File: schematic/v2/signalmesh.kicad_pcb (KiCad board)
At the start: 4 copper layers, 387 x 151 mm, 188 parts, among them J1 FPGA I/O, J10 INA219_CONFIG, J11 INA219_CONFIG, J12 AAM_DBG, J13 UUM_DBG, J14 ACM_DBG, J15 INA219_CONFIG, J16 DSM_DBG, J17 LCD_display, J18 LCD_display, J19 AudioJack3, J2 FPGA I/O, J20 USB_A, J21 USB_A, J22 USB_A, J23 USB_A, J3 LCD_display, J4 TDM_DBG, J5 INA219_CONFIG, J6 INA219_CONFIG, J7 INA219_CONFIG, J8 FPGA I/O, J9 FPGA I/O, U1 NUCLEO-H753ZI, U10 INA219AxD, U11 INA219AxD, U12 INA219AxD, U13 INA219AxD, U14 W25Q128JVS, U15 AP2112K-3.3, U16 74HC4050D, U17 NUCLEO-H753ZI, U18 HDSP-7503, U19 HDSP-7503, U2 HDSP-7503, U20 INA219AxD, U21 74HC4050D, U22 AP2112K-3.3, U23 W25Q128JVS, U24 74HC4050D, U25 AP2112K-3.3, U26 W25Q128JVS, U27 MCP2551-I-P, U28 74LVC1G3157, U29 MCP2551-I-P, U3 NUCLEO-F303RE, U30 MCP2551-I-P, U31 MCP2551-I-P, U33 CH340G, U4 YAAJ_BluePill_Part_Like, U5 24LC256-I_SN, U6 BME280, U7 INA219AxD, U8 24LC256-I_SN, U9 NUCLEO-F446RE

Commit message: time to start routing?
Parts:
- removed 5V_TDM_TEST, 5V_UUM, AAM_DAC_L, AAM_DAC_R, ACM_VDD, DSM_VDD, GND, TDM_I2C1_SCL, TDM_I2C1_SDA, VDD_UUM: TestPoint_Keystone_5019_Miniature, TestPoint:TestPoint_Keystone_5019_Miniature
- removed C11, C12, C13, C14, C15, C16: 22pf, Capacitor_SMD:C_0805_2012Metric
- removed D33, D34, D39: LED_PWR, LED_SMD:LED_0603_1608Metric
- removed D35, D40: TXD, LED_SMD:LED_0603_1608Metric
- removed D36, D41: RXD, LED_SMD:LED_0603_1608Metric
- removed J12: AAM_DBG, Connector_PinHeader_1.00mm:PinHeader_1x03_P1.00mm_Horizontal
- removed J13: UUM_DBG, Connector_PinHeader_1.00mm:PinHeader_1x03_P1.00mm_Horizontal
- removed J14: ACM_DBG, Connector_PinHeader_1.00mm:PinHeader_1x03_P1.00mm_Horizontal
- removed J16: DSM_DBG, Connector_PinHeader_1.00mm:PinHeader_1x03_P1.00mm_Horizontal
- removed J17: LCD_display, Connector_PinHeader_1.00mm:PinHeader_1x04_P1.00mm_Vertical_SMD_Pin1Left
- removed J20, J23: USB_A, Connector_USB:USB_A_CNCTech_1001-011-01101_Horizontal
- removed R51, R52, R53, R54, R57, R58, R59, R60: 300, Resistor_SMD:R_0805_2012Metric_Pad1.20x1.40mm_HandSolder
- removed R55, R61: 1k5, Resistor_SMD:R_0805_2012Metric_Pad1.20x1.40mm_HandSolder
- removed U33: CH340G, Package_SO:SOIC-16_3.9x9.9mm_P1.27mm
- added C23: 22pf, Capacitor_SMD:C_0805_2012Metric, F.Cu at (376.1, 151.8)
- added C24: 22pf, Capacitor_SMD:C_0805_2012Metric, F.Cu at (380.9, 151.8)
- added C25: 22pf, Capacitor_SMD:C_0805_2012Metric, F.Cu at (396.4, 177.4)
- added C26: 22pf, Capacitor_SMD:C_0805_2012Metric, F.Cu at (501.5, 35.5)
- added C27: 22pf, Capacitor_SMD:C_0805_2012Metric, F.Cu at (517.0, 61.1)
- added C28: 22pf, Capacitor_SMD:C_0805_2012Metric, F.Cu at (521.8, 61.1)
- added C29: 22pf, Capacitor_SMD:C_0805_2012Metric, F.Cu at (290.6, 35.4)
- added C30: 22pf, Capacitor_SMD:C_0805_2012Metric, F.Cu at (306.0, 61.0)
- added C31: 22pf, Capacitor_SMD:C_0805_2012Metric, F.Cu at (310.8, 61.0)
- added C32: 22pf, Capacitor_SMD:C_0805_2012Metric, F.Cu at (425.2, 35.4)
- added C33: 22pf, Capacitor_SMD:C_0805_2012Metric, F.Cu at (440.7, 61.0)
- added C34: 22pf, Capacitor_SMD:C_0805_2012Metric, F.Cu at (445.5, 61.0)
- added C35: 22pf, Capacitor_SMD:C_0805_2012Metric, F.Cu at (208.7, 35.1)
- added C36: 22pf, Capacitor_SMD:C_0805_2012Metric, F.Cu at (224.1, 60.7)
- added C37: 22pf, Capacitor_SMD:C_0805_2012Metric, F.Cu at (228.9, 60.7)
- added D51: LED_PWR, LED_SMD:LED_0603_1608Metric, F.Cu at (525.4, 95.5)
- added D52: LED_PWR, LED_SMD:LED_0603_1608Metric, F.Cu at (525.3, 103.6)
- added D53: LED_PWR, LED_SMD:LED_0603_1608Metric, F.Cu at (381.1, 170.7)
- added D54: RXD, LED_SMD:LED_0603_1608Metric, F.Cu at (381.1, 163.9)
- added D55: TXD, LED_SMD:LED_0603_1608Metric, F.Cu at (381.1, 167.4)
- added D56: LED_PWR, LED_SMD:LED_0603_1608Metric, F.Cu at (501.5, 38.8)
- added D57: LED_PWR, LED_SMD:LED_0603_1608Metric, F.Cu at (516.8, 42.2)
- added D58: TXD, LED_SMD:LED_0603_1608Metric, F.Cu at (516.8, 45.5)
- added D59: RXD, LED_SMD:LED_0603_1608Metric, F.Cu at (516.8, 49.0)
- added D60: LED_PWR, LED_SMD:LED_0603_1608Metric, F.Cu at (290.6, 38.6)
- added D61: LED_PWR, LED_SMD:LED_0603_1608Metric, F.Cu at (305.8, 42.1)
- added D62: TXD, LED_SMD:LED_0603_1608Metric, F.Cu at (305.8, 45.4)
- added D63: RXD, LED_SMD:LED_0603_1608Metric, F.Cu at (305.8, 48.9)
- added D64: LED_PWR, LED_SMD:LED_0603_1608Metric, F.Cu at (425.2, 38.6)
- added D65: LED_PWR, LED_SMD:LED_0603_1608Metric, F.Cu at (440.5, 42.1)
- added D66: TXD, LED_SMD:LED_0603_1608Metric, F.Cu at (440.5, 45.4)
- added D67: RXD, LED_SMD:LED_0603_1608Metric, F.Cu at (440.5, 48.9)
- added D68: LED_PWR, LED_SMD:LED_0603_1608Metric, F.Cu at (208.7, 38.4)
- added D69: LED_PWR, LED_SMD:LED_0603_1608Metric, F.Cu at (223.9, 41.9)
- added D70: TXD, LED_SMD:LED_0603_1608Metric, F.Cu at (223.9, 45.1)
- added D71: RXD, LED_SMD:LED_0603_1608Metric, F.Cu at (223.9, 48.6)
- added J25: USB_A, Connector_USB:USB_A_CNCTech_1001-011-01101_Horizontal, F.Cu at (385.6, 185.4)
- added J26: UART_DEBUG, Connector_PinHeader_1.00mm:PinHeader_1x03_P1.00mm_Horizontal, F.Cu at (370.2, 177.9)
- added J27: USB_A, Connector_USB:USB_A_CNCTech_1001-011-01101_Horizontal, F.Cu at (512.2, 27.5)
- added J28: UART_DEBUG, Connector_PinHeader_1.00mm:PinHeader_1x03_P1.00mm_Horizontal, F.Cu at (527.6, 35.0)
- added J29: USB_A, Connector_USB:USB_A_CNCTech_1001-011-01101_Horizontal, F.Cu at (301.3, 27.4)
- added J30: UART_DEBUG, Connector_PinHeader_1.00mm:PinHeader_1x03_P1.00mm_Horizontal, F.Cu at (316.6, 34.9)
- added J31: USB_A, Connector_USB:USB_A_CNCTech_1001-011-01101_Horizontal, F.Cu at (436.0, 27.4)
- added J32: UART_DEBUG, Connector_PinHeader_1.00mm:PinHeader_1x03_P1.00mm_Horizontal, F.Cu at (451.4, 34.9)
- added J33: USB_A, Connector_USB:USB_A_CNCTech_1001-011-01101_Horizontal, F.Cu at (219.4, 27.1)
- added J34: UART_DEBUG, Connector_PinHeader_1.00mm:PinHeader_1x03_P1.00mm_Horizontal, F.Cu at (234.8, 34.6)
- added R100: 1k5, Resistor_SMD:R_0805_2012Metric_Pad1.20x1.40mm_HandSolder, F.Cu at (234.7, 38.9)
- added R101: 300, Resistor_SMD:R_0805_2012Metric_Pad1.20x1.40mm_HandSolder, F.Cu at (227.9, 45.1)
- added R102: 300, Resistor_SMD:R_0805_2012Metric_Pad1.20x1.40mm_HandSolder, F.Cu at (227.9, 48.6)
- added R72: 300, Resistor_SMD:R_0805_2012Metric_Pad1.20x1.40mm_HandSolder, F.Cu at (392.4, 174.2)
- added R73: 10k, Resistor_SMD:R_0805_2012Metric_Pad1.20x1.40mm_HandSolder, F.Cu at (490.6, 145.4)
- added R74: 10k, Resistor_SMD:R_0805_2012Metric_Pad1.20x1.40mm_HandSolder, F.Cu at (490.6, 116.4)
- added R75: 10k, Resistor_SMD:R_0805_2012Metric_Pad1.20x1.40mm_HandSolder, F.Cu at (523.8, 116.7)
- added R76: 10k, Resistor_SMD:R_0805_2012Metric_Pad1.20x1.40mm_HandSolder, F.Cu at (523.8, 145.4)
- added R77: 300, Resistor_SMD:R_0805_2012Metric_Pad1.20x1.40mm_HandSolder, F.Cu at (521.4, 95.5)
- added R78: 300, Resistor_SMD:R_0805_2012Metric_Pad1.20x1.40mm_HandSolder, F.Cu at (521.4, 103.5)
- added R79: 300, Resistor_SMD:R_0805_2012Metric_Pad1.20x1.40mm_HandSolder, F.Cu at (377.1, 170.7)
- added R80: 300, Resistor_SMD:R_0805_2012Metric_Pad1.20x1.40mm_HandSolder, F.Cu at (377.1, 167.4)
- added R81: 1k5, Resistor_SMD:R_0805_2012Metric_Pad1.20x1.40mm_HandSolder, F.Cu at (370.4, 173.1)
- added R82: 300, Resistor_SMD:R_0805_2012Metric_Pad1.20x1.40mm_HandSolder, F.Cu at (377.1, 163.9)
- added R83: 300, Resistor_SMD:R_0805_2012Metric_Pad1.20x1.40mm_HandSolder, F.Cu at (505.5, 38.8)
- added R84: 300, Resistor_SMD:R_0805_2012Metric_Pad1.20x1.40mm_HandSolder, F.Cu at (520.8, 42.2)
- added R85: 1k5, Resistor_SMD:R_0805_2012Metric_Pad1.20x1.40mm_HandSolder, F.Cu at (527.5, 39.2)
- added R86: 300, Resistor_SMD:R_0805_2012Metric_Pad1.20x1.40mm_HandSolder, F.Cu at (520.8, 45.5)
- added R87: 300, Resistor_SMD:R_0805_2012Metric_Pad1.20x1.40mm_HandSolder, F.Cu at (520.8, 49.0)
- added R88: 300, Resistor_SMD:R_0805_2012Metric_Pad1.20x1.40mm_HandSolder, F.Cu at (294.6, 38.6)
- added R89: 300, Resistor_SMD:R_0805_2012Metric_Pad1.20x1.40mm_HandSolder, F.Cu at (309.8, 42.1)
- added R90: 1k5, Resistor_SMD:R_0805_2012Metric_Pad1.20x1.40mm_HandSolder, F.Cu at (316.6, 39.8)
- added R91: 300, Resistor_SMD:R_0805_2012Metric_Pad1.20x1.40mm_HandSolder, F.Cu at (309.8, 45.4)
- added R92: 300, Resistor_SMD:R_0805_2012Metric_Pad1.20x1.40mm_HandSolder, F.Cu at (309.8, 48.9)
- added R93: 300, Resistor_SMD:R_0805_2012Metric_Pad1.20x1.40mm_HandSolder, F.Cu at (429.2, 38.6)
- added R94: 300, Resistor_SMD:R_0805_2012Metric_Pad1.20x1.40mm_HandSolder, F.Cu at (444.5, 42.1)
- added R95: 1k5, Resistor_SMD:R_0805_2012Metric_Pad1.20x1.40mm_HandSolder, F.Cu at (451.2, 39.8)
- added R96: 300, Resistor_SMD:R_0805_2012Metric_Pad1.20x1.40mm_HandSolder, F.Cu at (444.5, 45.4)
- added R97: 300, Resistor_SMD:R_0805_2012Metric_Pad1.20x1.40mm_HandSolder, F.Cu at (444.5, 48.9)
- added R98: 300, Resistor_SMD:R_0805_2012Metric_Pad1.20x1.40mm_HandSolder, F.Cu at (212.7, 38.4)
- added R99: 300, Resistor_SMD:R_0805_2012Metric_Pad1.20x1.40mm_HandSolder, F.Cu at (227.9, 41.9)
- added U36: SM420561N, Display_7Segment:7SegmentLED_LTS6760_LTS6780, F.Cu at (188.5, 146.5)
- added U37: CH340G, Package_SO:SOIC-16_3.9x9.9mm_P1.27mm, F.Cu at (529.0, 48.7)
- added U38: CH340G, Package_SO:SOIC-16_3.9x9.9mm_P1.27mm, F.Cu at (318.0, 48.6)
- added U39: CH340G, Package_SO:SOIC-16_3.9x9.9mm_P1.27mm, F.Cu at (452.7, 48.6)
- added U40: CH340G, Package_SO:SOIC-16_3.9x9.9mm_P1.27mm, F.Cu at (236.1, 48.3)
- added Y2: 12MHz, Crystal:Crystal_HC49-4H_Vertical, F.Cu at (381.8, 158.4)
- added Y5: 12MHz, Crystal:Crystal_HC49-4H_Vertical, F.Cu at (516.1, 54.5)
- added Y7: 12MHz, Crystal:Crystal_HC49-4H_Vertical, F.Cu at (305.1, 54.4)
- added Y8: 12MHz, Crystal:Crystal_HC49-4H_Vertical, F.Cu at (439.8, 54.4)
- added Y9: 12MHz, Crystal:Crystal_HC49-4H_Vertical, F.Cu at (223.2, 54.1)
- D27: value LED_PWR -> SPI_SEL
- J18, J3: footprint Connector_PinHeader_1.00mm:PinHeader_1x04_P1.00mm_Vertical_SMD_Pin1Left -> Connector_PinHeader_1.00mm:PinHeader_1x04_P1.00mm_Horizontal
- J4: value TDM_DBG -> LCD_display; footprint Connector_PinHeader_1.00mm:PinHeader_1x03_P1.00mm_Horizontal -> Connector_PinHeader_1.00mm:PinHeader_1x04_P1.00mm_Horizontal
- U18, U2: value HDSP-7503 -> SM420561N; footprint Display_7Segment:HDSP-A151 -> Display_7Segment:7SegmentLED_LTS6760_LTS6780
- U19: value HDSP-7503 -> CH340G; footprint Display_7Segment:HDSP-A151 -> Package_SO:SOIC-16_3.9x9.9mm_P1.27mm
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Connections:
- net AAM_CAN_RD renamed /APM_CAN_RD
- net AAM_CAN_TD renamed /APM_CAN_TD
- net AAM_CMD_RX renamed /ACM_CMD_RX
- net AAM_CMD_TX renamed /ACM_CMD_TX
- net AAM_DAC_L renamed /DAC_L
- net AAM_DAC_R renamed /DAC_R
- net AAM_INTRPT_RX renamed /ISR0
- net AAM_INTRPT_TX renamed /IRQ0
- net AAM_LED_FAIL renamed /APM/APM_LED_FAIL
- net AAM_LED_OK renamed /APM/APM_LED_OK
- net AAM_LED_WARN renamed /APM/APM_LED_WARN
- net AAM_USB_D+ renamed /APM/APM_USB_D+
- net AAM_USB_D- renamed /APM/APM_USB_D-
- net ACM_LED_FAIL renamed /ACM/ACM_LED_FAIL
- net ACM_LED_OK renamed /ACM/ACM_LED_OK
- net ACM_LED_WARN renamed /ACM/ACM_LED_WARN
- net ACM_SPI_CS renamed /ACM/ACM_SPI_CS
- net ACM_SPI_MISO renamed /ACM/ACM_SPI_MISO
- net ACM_SPI_MOSI renamed /ACM/ACM_SPI_MOSI
- net ACM_SPI_SCLK renamed /ACM/ACM_SPI_SCLK
- net DSM_CAN_RD renamed /DSM_CAN_RD
- net DSM_CAN_TD renamed /DSM_CAN_TD
- net DSM_LED_FAIL renamed /DSM/DSM_LED_FAIL
- net DSM_LED_OK renamed /DSM/DSM_LED_OK
- net DSM_LED_WARN renamed /DSM/DSM_LED_WARN
- net TDM_CAN_RD renamed /TDM_CAN_RD
- net TDM_CAN_TD renamed /TDM_CAN_TD
- net TDM_I2C1_SCL renamed /TDM/TDM_I2C1_SCL
- net TDM_I2C1_SDA renamed /TDM/TDM_I2C1_SDA
- net TDM_LED_FAIL renamed /TDM/TDM_LED_FAIL
- net TDM_LED_OK renamed /TDM/TDM_LED_OK
- net TDM_LED_WARN renamed /TDM/TDM_LED_WARN
- net UUM_LED_FAIL renamed /UUM/UUM_LED_FAIL
- net UUM_LED_OK renamed /UUM/UUM_LED_OK
- net UUM_LED_WARN renamed /UUM/UUM_LED_WARN
- net UUM_SPI1_CS renamed /UUM/UUM_SPI1_CS
- net UUM_SPI1_MISO_B renamed /UUM/UUM_spiflash/UUM_SPI1_MISO_B
- net UUM_SPI1_MOSI renamed /UUM/UUM_SPI1_MOSI
- net UUM_SPI2_CS renamed /UUM/UUM_SPI2_CS
- net UUM_SPI_SEL renamed /UUM/UUM_SPI_SEL
- net VDD_7SDD renamed /TDM/7SDD_VDD
- C10 pad 1: 3V3_UUM -> Net-(C10-Pad1)
- J1 pad 18: AAM_FMC_CLK -> /FMC_CLK
- J1 pad 19: AAM_FMC_NWE -> /FMC_NWE
- J1 pad 20: AAM_FMC_NOE -> /FMC_NOE
- J1 pad 21: AAM_FMC_NE -> /FMC_NE
- J1 pad 22: AAM_FMC_NL -> /FMC_NL
- J1 pad 23: AAM_FMC_NBL0 -> /FMC_NBL0
- J1 pad 24: AAM_FMC_NBL1 -> /FMC_NBL1
- J1 pad 5: ACM_DBG_TX -> /ACM_DBG_TX
- J1 pad 6: ACM_DBG_RX -> /ACM_DBG_RX
- J2 pad 1: AAM_FMC_D0 -> /FMC_D0
- J2 pad 10: AAM_FMC_D9 -> /FMC_D9
- J2 pad 11: AAM_FMC_D10 -> /FMC_D10
- J2 pad 12: AAM_FMC_D11 -> /FMC_D11
- J2 pad 13: AAM_FMC_D12 -> /FMC_D12
- J2 pad 14: AAM_FMC_D13 -> /FMC_D13
- J2 pad 15: ACM_FMC_D14 -> /FMC_D14
- J2 pad 16: ACM_FMC_D15 -> /FMC_D15
- J2 pad 18: 5V_ACM -> ACM_VDD
- J2 pad 2: AAM_FMC_D1 -> /FMC_D1
- J2 pad 3: AAM_FMC_D2 -> /FMC_D2
- J2 pad 4: AAM_FMC_D3 -> /FMC_D3
- J2 pad 5: AAM_FMC_D4 -> /FMC_D4
- J2 pad 6: AAM_FMC_D5 -> /FMC_D5
- J2 pad 7: AAM_FMC_D6 -> /FMC_D6
- J2 pad 8: AAM_FMC_D7 -> /FMC_D7
- J2 pad 9: AAM_FMC_D8 -> /FMC_D8
- J21 pad 1: AAM_VDD -> APM_VDD
- J22 pad 2: DSM_USB_D- -> /DSM/DSM_USB_D-
- J22 pad 3: DSM_USB_D+ -> /DSM/DSM_USB_D+
- J3 pad 1: AAM_VDD -> DSM_VDD
- J3 pad 2: AAM_I2C1_SDA -> /DSM/DSM_I2C1_SDA
- J3 pad 3: AAM_I2C1_SCL -> /DSM/DSM_I2C1_SCL
- J4 pad 1: TDM_DBG_TX -> APM_VDD
- J4 pad 2: TDM_DBG_RX -> /APM/APM_I2C1_SDA
- J4 pad 3: GND -> /APM/APM_I2C1_SCL
- J8 pad 18: AAM_FMC_CLK -> /FMC_CLK
- J8 pad 19: AAM_FMC_NWE -> /FMC_NWE
- J8 pad 20: AAM_FMC_NOE -> /FMC_NOE
- J8 pad 21: AAM_FMC_NE -> /FMC_NE
- J8 pad 22: AAM_FMC_NL -> /FMC_NL
- J8 pad 23: AAM_FMC_NBL0 -> /FMC_NBL0
- J8 pad 24: AAM_FMC_NBL1 -> /FMC_NBL1
- J8 pad 5: ACM_DBG_TX -> /ACM_DBG_TX
- J8 pad 6: ACM_DBG_RX -> /ACM_DBG_RX
- J9 pad 1: AAM_FMC_D0 -> /FMC_D0
- J9 pad 10: AAM_FMC_D9 -> /FMC_D9
- J9 pad 11: AAM_FMC_D10 -> /FMC_D10
- J9 pad 12: AAM_FMC_D11 -> /FMC_D11
- J9 pad 13: AAM_FMC_D12 -> /FMC_D12
- J9 pad 14: AAM_FMC_D13 -> /FMC_D13
- J9 pad 15: ACM_FMC_D14 -> /FMC_D14
- J9 pad 16: ACM_FMC_D15 -> /FMC_D15
- J9 pad 17: unconnected-(J9-Pin_17-Pad17) -> unconnected-(J2-Pin_17-Pad17)
- J9 pad 18: 5V_ACM -> ACM_VDD
- J9 pad 2: AAM_FMC_D1 -> /FMC_D1
- J9 pad 3: AAM_FMC_D2 -> /FMC_D2
- J9 pad 4: AAM_FMC_D3 -> /FMC_D3
- J9 pad 5: AAM_FMC_D4 -> /FMC_D4
- J9 pad 6: AAM_FMC_D5 -> /FMC_D5
- J9 pad 7: AAM_FMC_D6 -> /FMC_D6
- J9 pad 8: AAM_FMC_D7 -> /FMC_D7
- J9 pad 9: AAM_FMC_D8 -> /FMC_D8
- R11 pad 2: 5V_TDM -> TDM_VDD
- R12 pad 2: 5V_TDM -> TDM_VDD
- R29 pad 2: VDD_ACM -> /TDM/ACM_VDD
- R30 pad 2: VDD_AAM -> /TDM/APM_VDD
- R31 pad 2: VDD_UUM -> /TDM/UUM_VDD
- R32 pad 2: VDD_DSM -> /TDM/DSM_VDD
- R38 pad 2: AAM_VDD -> APM_VDD
- R42 pad 1: Net-(U28B-VCC) -> UUM_3v3
- R42 pad 2: 3V3_UUM -> Net-(C10-Pad1)
- R50 pad 2: AAM_VDD -> APM_VDD
- U1 pad CN10_1: unconnected-(U1F-AVDD-PadCN10_1) -> (no net)
- U1 pad CN10_10: unconnected-(U1F-D3/TIMER_A_PWM3-PadCN10_10) -> (no net)
- U1 pad CN10_11: unconnected-(U1F-A8/ADC_C_IN-PadCN10_11) -> (no net)
- U1 pad CN10_12: unconnected-(U1F-D2/IO-PadCN10_12) -> (no net)
- U1 pad CN10_13: unconnected-(U1F-D26/QSPI_CS-PadCN10_13) -> (no net)
- U1 pad CN10_14: unconnected-(U1F-D1/USART_A_TX-PadCN10_14) -> (no net)
- U1 pad CN10_15: unconnected-(U1F-D27/QSPI_CLK-PadCN10_15) -> (no net)
- U1 pad CN10_16: unconnected-(U1F-D0/USART_A_RX-PadCN10_16) -> (no net)
- U1 pad CN10_17: Net-(U1F-GND_CN10-PadCN10_17) -> (no net)
- U1 pad CN10_18: unconnected-(U1F-D42/TIMER_A_PWM1N-PadCN10_18) -> (no net)
- U1 pad CN10_19: unconnected-(U1F-D28/QSPI_BK1_IO3-PadCN10_19) -> (no net)
- U1 pad CN10_2: unconnected-(U1F-D7/IO-PadCN10_2) -> (no net)
- U1 pad CN10_20: unconnected-(U1F-D41/TIMER_A_ETR-PadCN10_20) -> (no net)
- U1 pad CN10_21: unconnected-(U1F-D29/QSPI_BK1_IO1-PadCN10_21) -> (no net)
- U1 pad CN10_22: Net-(U1F-GND_CN10-PadCN10_17) -> (no net)
- U1 pad CN10_23: unconnected-(U1F-D30/QSPI_BK1_IO0-PadCN10_23) -> (no net)
- U1 pad CN10_24: unconnected-(U1F-D40/TIMER_A_PWM2N-PadCN10_24) -> (no net)
- U1 pad CN10_25: unconnected-(U1F-D31/QSPI_BK1_IO2-PadCN10_25) -> (no net)
- U1 pad CN10_26: unconnected-(U1F-D39/TIMER_A_PWM3N-PadCN10_26) -> (no net)
- U1 pad CN10_27: Net-(U1F-GND_CN10-PadCN10_17) -> (no net)
- U1 pad CN10_28: unconnected-(U1F-D38/TIMER_A_BKIN2-PadCN10_28) -> (no net)
- U1 pad CN10_29: unconnected-(U1F-D32/TIMER_C_PWM1-PadCN10_29) -> (no net)
- U1 pad CN10_3: unconnected-(U1F-AGND_CN10-PadCN10_3) -> (no net)
- U1 pad CN10_30: unconnected-(U1F-D37/TIMER_A_BKIN1-PadCN10_30) -> (no net)
- U1 pad CN10_31: unconnected-(U1F-D33/TIMER_D_PWM1-PadCN10_31) -> (no net)
- U1 pad CN10_32: unconnected-(U1F-D36/TIMER_C_PWM2-PadCN10_32) -> (no net)
- U1 pad CN10_33: unconnected-(U1F-D34/TIMER_B_ETR-PadCN10_33) -> (no net)
- U1 pad CN10_34: unconnected-(U1F-D35/TIMER_C_PWM3-PadCN10_34) -> (no net)
- U1 pad CN10_4: unconnected-(U1F-D6/TIMER_A_PWM1-PadCN10_4) -> (no net)
- U1 pad CN10_5: Net-(U1F-GND_CN10-PadCN10_17) -> (no net)
- U1 pad CN10_6: unconnected-(U1F-D5/TIMER_A_PWM2-PadCN10_6) -> (no net)
- U1 pad CN10_7: unconnected-(U1F-A6/ADC_A_IN-PadCN10_7) -> (no net)
- U1 pad CN10_8: unconnected-(U1F-D4/IO-PadCN10_8) -> (no net)
- U1 pad CN10_9: unconnected-(U1F-A7/ADC_B_IN-PadCN10_9) -> (no net)
- U1 pad CN11_18: 5V_AAM -> APM_VDD
- U1 pad CN11_21: AAM_FMC_NL -> unconnected-(U1A-PB7-PadCN11_21)
- U1 pad CN11_3: AAM_DBG_TX -> /APM_DBG_TX
- U1 pad CN11_39: AAM_FMC_NOE -> unconnected-(U1A-PD4-PadCN11_39)
- U1 pad CN11_4: AAM_DBG_RX -> /APM_DBG_RX
- U1 pad CN11_40: AAM_FMC_CLK -> unconnected-(U1A-PD3-PadCN11_40)
- U1 pad CN11_41: AAM_FMC_NWE -> unconnected-(U1A-PD5-PadCN11_41)
- U1 pad CN11_51: unconnected-(U1A-PF1-PadCN11_51) -> /APM/APM_I2C1_SCL
- U1 pad CN11_53: unconnected-(U1A-PF0-PadCN11_53) -> /APM/APM_I2C1_SDA
- U1 pad CN11_55: AAM_FMC_D3 -> unconnected-(U1A-PD1-PadCN11_55)
- U1 pad CN11_57: AAM_FMC_D2 -> unconnected-(U1A-PD0-PadCN11_57)
- U1 pad CN11_61: AAM_FMC_NBL1 -> unconnected-(U1A-PE1-PadCN11_61)
- U1 pad CN11_63: unconnected-(U1A-PG9-PadCN11_63) -> /APM/7SDD_CMD_RX
- U1 pad CN11_69: ACM_FMC_D14 -> unconnected-(U1A-PD9-PadCN11_69)
- U1 pad CN12_10: AAM_FMC_D13 -> unconnected-(U1B-PD8-PadCN12_10)
- U1 pad CN12_19: AAM_FMC_NE -> unconnected-(U1B-PC7-PadCN12_19)
- U1 pad CN12_20: Net-(U1B-GND_CN12-PadCN12_20) -> unconnected-(U1B-GND_CN12-PadCN12_20)_4
- U1 pad CN12_39: Net-(U1B-GND_CN12-PadCN12_20) -> unconnected-(U1B-GND_CN12-PadCN12_20)_1
- U1 pad CN12_40: AAM_FMC_D5 -> unconnected-(U1B-PE8-PadCN12_40)
- U1 pad CN12_44: AAM_FMC_D4 -> unconnected-(U1B-PE7-PadCN12_44)
- U1 pad CN12_46: AAM_FMC_D0 -> unconnected-(U1B-PD14-PadCN12_46)
- U1 pad CN12_47: AAM_FMC_D7 -> unconnected-(U1B-PE10-PadCN12_47)
- U1 pad CN12_48: AAM_FMC_D1 -> unconnected-(U1B-PD15-PadCN12_48)
- U1 pad CN12_49: AAM_FMC_D9 -> unconnected-(U1B-PE12-PadCN12_49)
- U1 pad CN12_51: AAM_FMC_D11 -> unconnected-(U1B-PE14-PadCN12_51)
- U1 pad CN12_52: AAM_FMC_D6 -> unconnected-(U1B-PE9-PadCN12_52)
- U1 pad CN12_53: AAM_FMC_D12 -> unconnected-(U1B-PE15-PadCN12_53)
- U1 pad CN12_54: Net-(U1B-GND_CN12-PadCN12_20) -> unconnected-(U1B-GND_CN12-PadCN12_20)
- U1 pad CN12_55: AAM_FMC_D10 -> unconnected-(U1B-PE13-PadCN12_55)
- U1 pad CN12_56: AAM_FMC_D8 -> unconnected-(U1B-PE11-PadCN12_56)
- U1 pad CN12_61: unconnected-(U1B-PG14-PadCN12_61) -> /APM/7SDD_CMD_TX
- U1 pad CN12_63: Net-(U1B-GND_CN12-PadCN12_20) -> unconnected-(U1B-GND_CN12-PadCN12_20)_3
- U1 pad CN12_64: AAM_FMC_NBL0 -> unconnected-(U1B-PE0-PadCN12_64)
- U1 pad CN12_65: ACM_FMC_D15 -> unconnected-(U1B-PD10-PadCN12_65)
- U1 pad CN12_71: Net-(U1B-GND_CN12-PadCN12_20) -> unconnected-(U1B-GND_CN12-PadCN12_20)_6
- U1 pad CN12_72: Net-(U1B-GND_CN12-PadCN12_20) -> unconnected-(U1B-GND_CN12-PadCN12_20)_5
- U1 pad CN12_9: Net-(U1B-GND_CN12-PadCN12_20) -> unconnected-(U1B-GND_CN12-PadCN12_20)_2
- U1 pad CN7_1: unconnected-(U1E-D16/I2S_A_MCK-PadCN7_1) -> (no net)
- U1 pad CN7_10: unconnected-(U1E-D13/SPI_A_SCK-PadCN7_10) -> (no net)
- U1 pad CN7_11: unconnected-(U1E-D21/I2S_B_MCK-PadCN7_11) -> (no net)
- U1 pad CN7_12: unconnected-(U1E-D12/SPI_A_MISO-PadCN7_12) -> (no net)
- U1 pad CN7_13: unconnected-(U1E-D22/I2S_B_SD/SPI_B_MOSI-PadCN7_13) -> (no net)
- U1 pad CN7_14: unconnected-(U1E-D11/SPI_A_MOSI/TIM_E_PWM1-PadCN7_14) -> (no net)
- U1 pad CN7_15: unconnected-(U1E-D23/I2S_B_CK/SPI_B_SCK-PadCN7_15) -> (no net)
- U1 pad CN7_16: unconnected-(U1E-D10/SPI_A_CS/TIM_B_PWM3-PadCN7_16) -> (no net)
- U1 pad CN7_17: unconnected-(U1E-D24/SPI_B_NSS-PadCN7_17) -> (no net)
- U1 pad CN7_18: unconnected-(U1E-D9/TIMER_B_PWM2-PadCN7_18) -> (no net)
- U1 pad CN7_19: unconnected-(U1E-D25/SPI_B_MISO-PadCN7_19) -> (no net)
- U1 pad CN7_2: unconnected-(U1E-D15/I2C_A_SCL-PadCN7_2) -> (no net)
- U1 pad CN7_20: unconnected-(U1E-D8/IO-PadCN7_20) -> (no net)
- U1 pad CN7_3: unconnected-(U1E-D17/I2S_A_SD-PadCN7_3) -> (no net)
- U1 pad CN7_4: unconnected-(U1E-D14/I2C_A_SDA-PadCN7_4) -> (no net)
- U1 pad CN7_5: unconnected-(U1E-D18/I2S_A_CK-PadCN7_5) -> (no net)
- U1 pad CN7_6: unconnected-(U1E-VREFP_CN7-PadCN7_6) -> (no net)
- U1 pad CN7_7: unconnected-(U1E-D19/I2S_A_WS-PadCN7_7) -> (no net)
- U1 pad CN7_8: unconnected-(U1E-GND_CN7-PadCN7_8) -> (no net)
- U1 pad CN7_9: unconnected-(U1E-D20/I2S_B_WS-PadCN7_9) -> (no net)
- U1 pad CN8_1: unconnected-(U1C-NC_CN8-PadCN8_1) -> (no net)
- U1 pad CN8_10: unconnected-(U1C-D47/SDMMC_CK-PadCN8_10) -> (no net)
- U1 pad CN8_11: Net-(U1C-GND_CN8-PadCN8_11) -> (no net)
- U1 pad CN8_12: unconnected-(U1C-D48/SDMMC_CMD-PadCN8_12) -> (no net)
- U1 pad CN8_13: Net-(U1C-GND_CN8-PadCN8_11) -> (no net)
- U1 pad CN8_14: unconnected-(U1C-D49/IO-PadCN8_14) -> (no net)
- U1 pad CN8_15: unconnected-(U1C-VIN_CN8-PadCN8_15) -> (no net)
- U1 pad CN8_16: unconnected-(U1C-D50/IO-PadCN8_16) -> (no net)
- U1 pad CN8_2: unconnected-(U1C-D43/SDMMC_D0-PadCN8_2) -> (no net)
- U1 pad CN8_3: unconnected-(U1C-IOREF_CN8-PadCN8_3) -> (no net)
- U1 pad CN8_4: unconnected-(U1C-D44/SDMMC_D1/I2S_A_CKIN-PadCN8_4) -> (no net)
- U1 pad CN8_5: unconnected-(U1C-NRST_CN8-PadCN8_5) -> (no net)
- U1 pad CN8_6: unconnected-(U1C-D45/SDMMC_D2-PadCN8_6) -> (no net)
- U1 pad CN8_7: unconnected-(U1C-3V3_CN8-PadCN8_7) -> (no net)
- U1 pad CN8_8: unconnected-(U1C-D46/SDMMC_D3-PadCN8_8) -> (no net)
- U1 pad CN8_9: unconnected-(U1C-5V_CN8-PadCN8_9) -> (no net)
- U1 pad CN9_1: unconnected-(U1D-A0/ADC12_INP15-PadCN9_1) -> (no net)
- U1 pad CN9_10: unconnected-(U1D-D55/USART_B_CTS-PadCN9_10) -> (no net)
- U1 pad CN9_11: unconnected-(U1D-A5/ADC3_INP6/I2C1_SCL-PadCN9_11) -> (no net)
- U1 pad CN9_12: Net-(U1D-GND_CN9-PadCN9_12) -> (no net)
- U1 pad CN9_13: unconnected-(U1D-D72/COMP1_INP-PadCN9_13) -> (no net)
- U1 pad CN9_14: unconnected-(U1D-D56/SAI_A_MCLK-PadCN9_14) -> (no net)
- U1 pad CN9_15: unconnected-(U1D-D71/COMP2_INP-PadCN9_15) -> (no net)
- U1 pad CN9_16: unconnected-(U1D-D57/SAI_A_FS-PadCN9_16) -> (no net)
- U1 pad CN9_17: unconnected-(U1D-D70/I2C_B_SMBA-PadCN9_17) -> (no net)
- U1 pad CN9_18: unconnected-(U1D-D58/SAI_A_SCK-PadCN9_18) -> (no net)
- U1 pad CN9_19: unconnected-(U1D-D69/I2C_B_SCL-PadCN9_19) -> (no net)
- U1 pad CN9_2: unconnected-(U1D-D51/USART_B_SCLK-PadCN9_2) -> (no net)
- U1 pad CN9_20: unconnected-(U1D-D59/SAI_A_SD-PadCN9_20) -> (no net)
- U1 pad CN9_21: unconnected-(U1D-D68/I2C_B_SDA-PadCN9_21) -> (no net)
- U1 pad CN9_22: unconnected-(U1D-D60/SAI_B_SD-PadCN9_22) -> (no net)
- U1 pad CN9_23: Net-(U1D-GND_CN9-PadCN9_12) -> (no net)
- U1 pad CN9_24: unconnected-(U1D-D61/SAI_B_SCK-PadCN9_24) -> (no net)
- U1 pad CN9_25: unconnected-(U1D-D67/CAN_RX-PadCN9_25) -> (no net)
- U1 pad CN9_26: unconnected-(U1D-D62/SAI_B_MCLK-PadCN9_26) -> (no net)
- U1 pad CN9_27: unconnected-(U1D-D66/CAN_TX-PadCN9_27) -> (no net)
- U1 pad CN9_28: unconnected-(U1D-D63/SAI_B_FS-PadCN9_28) -> (no net)
- U1 pad CN9_29: unconnected-(U1D-D65/IO-PadCN9_29) -> (no net)
- U1 pad CN9_3: unconnected-(U1D-A1/ADC123_INP10-PadCN9_3) -> (no net)
- U1 pad CN9_30: unconnected-(U1D-D64/IO-PadCN9_30) -> (no net)
- U1 pad CN9_4: unconnected-(U1D-D52/USART_B_RX-PadCN9_4) -> (no net)
- U1 pad CN9_5: unconnected-(U1D-A2/ADC12_INP13-PadCN9_5) -> (no net)
- U1 pad CN9_6: unconnected-(U1D-D53/USART_B_TX-PadCN9_6) -> (no net)
- U1 pad CN9_7: unconnected-(U1D-A3/ADC12_INP5-PadCN9_7) -> (no net)
- U1 pad CN9_8: unconnected-(U1D-D54/USART_B_RTS-PadCN9_8) -> (no net)
- U1 pad CN9_9: unconnected-(U1D-A4/ADC123_INP12/I2C1_SDA-PadCN9_9) -> (no net)
- U10 pad 7: VDD_ACM -> /TDM/ACM_VDD
- U11 pad 7: VDD_DSM -> /TDM/DSM_VDD
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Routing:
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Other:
- board size 387 x 151 mm -> 478 x 151.1 mm
- board text added: "APM DSPLY"
- board text added: "APM_DBG"
- board text added: "C8"
- board text added: "DSM DSPLY"
- board text added: "MEDIA OUT"
- board text added: "MIDI IN"
- board text added: "R10"
- board text added: "STM32H755 NUCLEO Audio Parameter Module APM"
- board text added: "TDM DSPLY"
- board text added: "U22"
- board text added: "signalmesh dev board v2.0 Akiel Aries 2025"
- board text removed: "AAM DSPLY"
- board text removed: "AAM_DBG"
- board text removed: "ACM_DBG"
- board text removed: "STM32H755 NUCLEO Audio Acquisition Module AAM"
- board text removed: "UUM_DBG"
- board text removed: "signalmesh dev board v2.0 by Akiel Aries 2025"

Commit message: gonna throw auto route on. I think I have enough put together for now
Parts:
- removed J19: AudioJack3, Connector_Audio:Jack_3.5mm_CUI_SJ-3523-SMT_Horizontal
- removed R19: 10k, Resistor_SMD:R_0805_2012Metric_Pad1.20x1.40mm_HandSolder
- added H3: Audio Thru, MountingHole:MountingHole_3.2mm_M3, F.Cu at (290.8, 163.6)
- added J12: AUDIO_OUT, Connector:NS-Tech_Grove_1x04_P2mm_Vertical, F.Cu at (293.8, 178.7)
- added R53: 10k, Resistor_SMD:R_0805_2012Metric_Pad1.20x1.40mm_HandSolder, F.Cu at (534.6, 61.6)
- added R54: 10k, Resistor_SMD:R_0805_2012Metric_Pad1.20x1.40mm_HandSolder, F.Cu at (451.5, 80.7)
- added R55: 10k, Resistor_SMD:R_0805_2012Metric_Pad1.20x1.40mm_HandSolder, F.Cu at (318.7, 81.1)
- added R57: 10k, Resistor_SMD:R_0805_2012Metric_Pad1.20x1.40mm_HandSolder, F.Cu at (241.4, 61.4)
- added REF**: KiCad-Logo2_5mm_SilkScreen, Symbol:KiCad-Logo2_5mm_SilkScreen, F.Cu at (552.5, 177.0)
- added REF**: OSHW-Logo_19x20mm_SilkScreen, Symbol:OSHW-Logo_19x20mm_SilkScreen, F.Cu at (559.5, 160.5)
- added TH2: 10k, Package_TO_SOT_THT:Heraeus_TO-92-2, F.Cu at (312.3, 80.7)
- added TH3: 10k, Package_TO_SOT_THT:Heraeus_TO-92-2, F.Cu at (235.0, 62.6)
- added TH4: 10k, Package_TO_SOT_THT:Heraeus_TO-92-2, F.Cu at (528.4, 61.6)
- added TP1: DAC_R_TP, TestPoint:TestPoint_THTPad_D2.5mm_Drill1.2mm, F.Cu at (293.2, 170.6)
- added TP2: DAC_L_TP, TestPoint:TestPoint_THTPad_D2.5mm_Drill1.2mm, F.Cu at (288.2, 170.6)
- TH1: footprint OptoDevice:R_LDR_4.9x4.2mm_P2.54mm_Vertical -> Package_TO_SOT_THT:Heraeus_TO-92-2
- moved TH1 113.3 mm to (445.1, 80.8)
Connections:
- TH1 pad 2: Net-(U9B-PC7) -> Net-(U9A-PC0/PB8)
- U9 pad CN10_19: Net-(U9B-PC7) -> unconnected-(U9B-PC7-PadCN10_19)
- U9 pad CN7_1: (no net) -> unconnected-(U9A-PC10-PadCN7_1)
- U9 pad CN7_12: (no net) -> unconnected-(U9A-CN7_IOREF-PadCN7_12)
- U9 pad CN7_13: (no net) -> unconnected-(U9A-PA13-PadCN7_13)
- U9 pad CN7_14: (no net) -> unconnected-(U9A-CN7_RESET-PadCN7_14)
- U9 pad CN7_15: (no net) -> unconnected-(U9A-PA14-PadCN7_15)
- U9 pad CN7_16: (no net) -> unconnected-(U9A-CN7_+3V3-PadCN7_16)
- U9 pad CN7_17: (no net) -> unconnected-(U9A-PA15-PadCN7_17)
- U9 pad CN7_18: (no net) -> unconnected-(U9A-CN7_+5V-PadCN7_18)
- U9 pad CN7_19: (no net) -> Net-(U9A-CN7_GND-PadCN7_19)
- U9 pad CN7_2: (no net) -> unconnected-(U9A-PC11-PadCN7_2)
- U9 pad CN7_20: (no net) -> Net-(U9A-CN7_GND-PadCN7_19)
- U9 pad CN7_21: (no net) -> unconnected-(U9A-PB7-PadCN7_21)
- U9 pad CN7_22: (no net) -> Net-(U9A-CN7_GND-PadCN7_19)
- U9 pad CN7_23: (no net) -> unconnected-(U9A-PC13-PadCN7_23)
- U9 pad CN7_24: (no net) -> unconnected-(U9A-CN7_VIN-PadCN7_24)
- U9 pad CN7_25: (no net) -> unconnected-(U9A-PC14-PadCN7_25)
- U9 pad CN7_27: (no net) -> unconnected-(U9A-PC15-PadCN7_27)
- U9 pad CN7_28: (no net) -> unconnected-(U9A-PA0-PadCN7_28)
- U9 pad CN7_29: (no net) -> unconnected-(U9A-PH0-PadCN7_29)
- U9 pad CN7_3: (no net) -> unconnected-(U9A-PC12-PadCN7_3)
- U9 pad CN7_30: (no net) -> unconnected-(U9A-PA1-PadCN7_30)
- U9 pad CN7_31: (no net) -> unconnected-(U9A-PH1-PadCN7_31)
- U9 pad CN7_32: (no net) -> Net-(U9A-PA4)
- U9 pad CN7_33: (no net) -> unconnected-(U9A-VBAT-PadCN7_33)
- U9 pad CN7_34: (no net) -> Net-(U9A-PB0)
- U9 pad CN7_35: (no net) -> unconnected-(U9A-PC2-PadCN7_35)
- U9 pad CN7_36: (no net) -> Net-(U9A-PC1/PB9)
- U9 pad CN7_37: (no net) -> unconnected-(U9A-PC3-PadCN7_37)
- U9 pad CN7_38: (no net) -> Net-(U9A-PC0/PB8)
- U9 pad CN7_4: (no net) -> unconnected-(U9A-PD2-PadCN7_4)
- U9 pad CN7_5: (no net) -> unconnected-(U9A-VDD-PadCN7_5)
- U9 pad CN7_6: (no net) -> unconnected-(U9A-E5V-PadCN7_6)
- U9 pad CN7_7: (no net) -> unconnected-(U9A-BOOT0-PadCN7_7)
- U9 pad CN7_8: (no net) -> Net-(U9A-CN7_GND-PadCN7_19)
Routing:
- net TDM_VDD: track 41.3 -> 159.8 mm
- net Net-(U9B-PC7): track 12.1 -> 0.00 mm
- net /DAC_L: track 0.00 -> 9.14 mm
- net /DAC_R: track 0.00 -> 9.07 mm
- net /TDM_DBG_RX: track 82.8 -> 91.7 mm, vias 2 -> 3
- net /TDM_DBG_TX: track 77.5 -> 83.5 mm, vias 0 -> 2
- net Net-(U9A-PC1/PB9): track 0.00 -> 2.66 mm
- net GND: track 133.7 -> 136.1 mm, vias 68 -> 69
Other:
- board size 478 x 151.1 mm -> 387 x 151 mm
- board text added: "signalmesh dev board v2.0 Akiel Aries 2025 github.com/akielaries/signalmesh"
- board text removed: "AUDIO OUT"
- board text removed: "signalmesh dev board v2.0 Akiel Aries 2025"

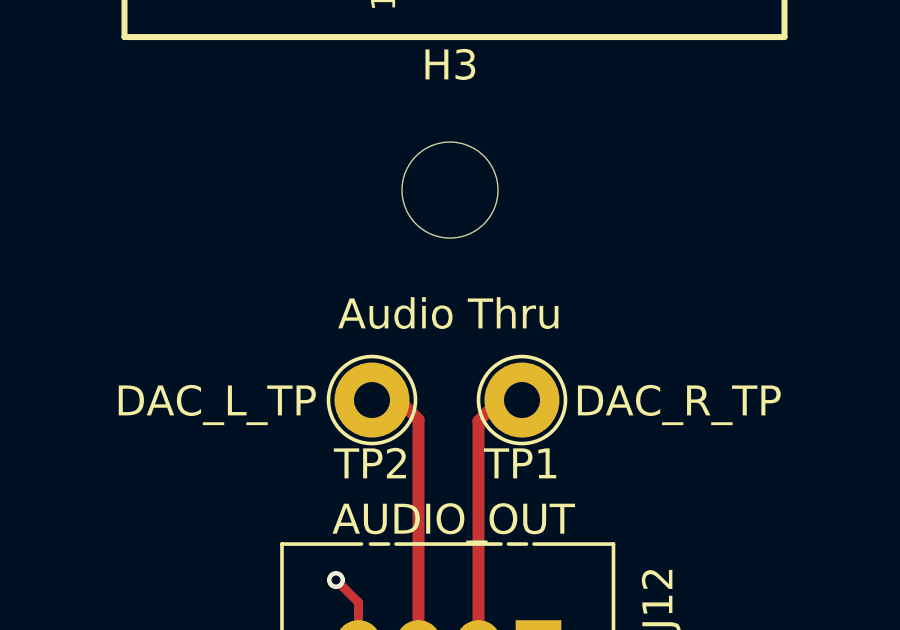
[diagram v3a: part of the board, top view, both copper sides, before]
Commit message: fixed designators
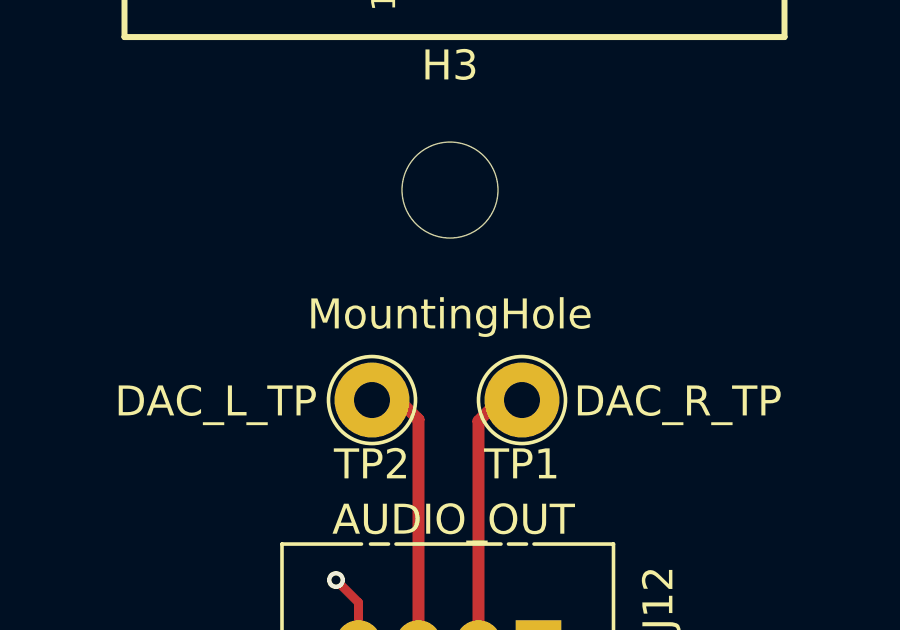
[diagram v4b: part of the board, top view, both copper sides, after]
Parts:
- H3: value Audio Thru -> MountingHole
- renumbered REF** to KiCAD_logo, REF** to OSHW
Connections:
- U9 pad CN7_19: Net-(U9A-CN7_GND-PadCN7_19) -> unconnected-(U9A-CN7_GND-PadCN7_19)_1
- U9 pad CN7_20: Net-(U9A-CN7_GND-PadCN7_19) -> unconnected-(U9A-CN7_GND-PadCN7_19)
- U9 pad CN7_22: Net-(U9A-CN7_GND-PadCN7_19) -> unconnected-(U9A-CN7_GND-PadCN7_19)_3
- U9 pad CN7_8: Net-(U9A-CN7_GND-PadCN7_19) -> unconnected-(U9A-CN7_GND-PadCN7_19)_2
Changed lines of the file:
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@@
 	(net 670 "unconnected-(U9A-CN7_IOREF-PadCN7_12)")
 	(net 671 "unconnected-(U9A-E5V-PadCN7_6)")
-	(net 672 "Net-(U9A-CN7_GND-PadCN7_19)")
-	(net 673 "unconnected-(U9A-CN7_+5V-PadCN7_18)")
-	(net 674 "unconnected-(U9A-BOOT0-PadCN7_7)")
-	(net 675 "unconnected-(U9A-CN7_+3V3-PadCN7_16)")
-	(net 676 "unconnected-(U9A-PD2-PadCN7_4)")
-	(net 677 "unconnected-(U9A-VBAT-PadCN7_33)")
-	(net 678 "unconnected-(U9A-PB7-PadCN7_21)")
-	(net 679 "unconnected-(U9A-PA13-PadCN7_13)")
-	(net 680 "unconnected-(U9A-CN7_VIN-PadCN7_24)")
-	(net 681 "unconnected-(U9A-PA14-PadCN7_15)")
-	(net 682 "unconnected-(U9A-PA1-PadCN7_30)")
-	(net 683 "unconnected-(U9A-VDD-PadCN7_5)")
-	(net 684 "unconnected-(U9A-PC2-PadCN7_35)")
-	(net 685 "unconnected-(U9B-PC7-PadCN10_19)")
-	(net 686 "unconnected-(U9A-PC15-PadCN7_27)")
-	(net 687 "unconnected-(U9A-PC10-PadCN7_1)")
-	(net 688 "unconnected-(U9A-PC12-PadCN7_3)")
-	(net 689 "unconnected-(J12-Pin_1-Pad1)")
+	(net 672 "unconnected-(U9A-CN7_+5V-PadCN7_18)")
+	(net 673 "unconnected-(U9A-BOOT0-PadCN7_7)")
+	(net 674 "unconnected-(U9A-CN7_+3V3-PadCN7_16)")
+	(net 675 "unconnected-(U9A-PD2-PadCN7_4)")
+	(net 676 "unconnected-(U9A-VBAT-PadCN7_33)")
+	(net 677 "unconnected-(U9A-PB7-PadCN7_21)")
+	(net 678 "unconnected-(U9A-PA13-PadCN7_13)")
+	(net 679 "unconnected-(U9A-CN7_VIN-PadCN7_24)")
+	(net 680 "unconnected-(U9A-PA14-PadCN7_15)")
+	(net 681 "unconnected-(U9A-PA1-PadCN7_30)")
+	(net 682 "unconnected-(U9A-VDD-PadCN7_5)")
+	(net 683 "unconnected-(U9A-PC2-PadCN7_35)")
+	(net 684 "unconnected-(U9B-PC7-PadCN10_19)")
+	(net 685 "unconnected-(U9A-PC15-PadCN7_27)")
+	(net 686 "unconnected-(U9A-PC10-PadCN7_1)")
+	(net 687 "unconnected-(U9A-PC12-PadCN7_3)")
+	(net 688 "unconnected-(J12-Pin_1-Pad1)")
+	(net 689 "unconnected-(U9A-CN7_GND-PadCN7_19)")
+	(net 690 "unconnected-(U9A-CN7_GND-PadCN7_19)_1")
+	(net 691 "unconnected-(U9A-CN7_GND-PadCN7_19)_2")
+	(net 692 "unconnected-(U9A-CN7_GND-PadCN7_19)_3")
 	(footprint "MountingHole:MountingHole_3.2mm_M3"
 		(layer "F.Cu")
@@
 			)
 		)
-		(property "Value" "Audio Thru"
+		(property "Value" "MountingHole"
 			(at 0 4.15 0)
 			(layer "F.SilkS")
@@
 		(descr "KiCad Logo")
 		(tags "Logo KiCad")
-		(property "Reference" "REF**"
+		(property "Reference" "KiCAD_logo"
 			(at 0 -5.08 0)
 			(layer "F.SilkS")
@@
 			(net 551 "unconnected-(U27-Vref-Pad5)")
 			(pinfunction "Vref")
-			(pintype "power_out+no_connect")
+			(pintype "power_out")
 		)
 		(pad "6" thru_hole circle
@@
 			(layers "*.Cu" "*.Mask")
 			(remove_unused_layers no)
-			(net 689 "unconnected-(J12-Pin_1-Pad1)")
+			(net 688 "unconnected-(J12-Pin_1-Pad1)")
 			(pinfunction "Pin_1")
 			(pintype "passive+no_connect")
@@
 		(descr "Open Source Hardware Logo")
 		(tags "Logo OSHW")
-		(property "Reference" "REF**"
+		(property "Reference" "OSHW"
 			(at 0 0 0)
 			(layer "F.SilkS")
@@
 			(net 552 "unconnected-(U29-Vref-Pad5)")
 			(pinfunction "Vref")
-			(pintype "power_out+no_connect")
+			(pintype "power_out")
 		)
 		(pad "6" thru_hole circle
@@
 			(layers "*.Cu" "*.Mask")
 			(remove_unused_layers no)
-			(net 687 "unconnected-(U9A-PC10-PadCN7_1)")
+			(net 686 "unconnected-(U9A-PC10-PadCN7_1)")
 			(pinfunction "PC10")
 			(pintype "bidirectional")
@@
 			(layers "*.Cu" "*.Mask")
 			(remove_unused_layers no)
-			(net 688 "unconnected-(U9A-PC12-PadCN7_3)")
+			(net 687 "unconnected-(U9A-PC12-PadCN7_3)")
 			(pinfunction "PC12")
 			(pintype "bidirectional")
@@
 			(layers "*.Cu" "*.Mask")
 			(remove_unused_layers no)
-			(net 676 "unconnected-(U9A-PD2-PadCN7_4)")
+			(net 675 "unconnected-(U9A-PD2-PadCN7_4)")
 			(pinfunction "PD2")
 			(pintype "bidirectional")
@@
 			(layers "*.Cu" "*.Mask")
 			(remove_unused_layers no)
-			(net 683 "unconnected-(U9A-VDD-PadCN7_5)")
+			(net 682 "unconnected-(U9A-VDD-PadCN7_5)")
 			(pinfunction "VDD")
-			(pintype "power_in")
+			(pintype "power_in+no_connect")
 			(solder_mask_margin 0.102)
 		)
@@
 			(net 671 "unconnected-(U9A-E5V-PadCN7_6)")
 			(pinfunction "E5V")
-			(pintype "power_in")
+			(pintype "power_in+no_connect")
 			(solder_mask_margin 0.102)
 		)
@@
 			(layers "*.Cu" "*.Mask")
 			(remove_unused_layers no)
-			(net 674 "unconnected-(U9A-BOOT0-PadCN7_7)")
+			(net 673 "unconnected-(U9A-BOOT0-PadCN7_7)")
 			(pinfunction "BOOT0")
 			(pintype "bidirectional")
@@
 			(layers "*.Cu" "*.Mask")
 			(remove_unused_layers no)
-			(net 672 "Net-(U9A-CN7_GND-PadCN7_19)")
+			(net 691 "unconnected-(U9A-CN7_GND-PadCN7_19)_2")
 			(pinfunction "CN7_GND")
-			(pintype "power_in")
+			(pintype "power_in+no_connect")
 			(solder_mask_margin 0.102)
 		)
@@
 			(layers "*.Cu" "*.Mask")
 			(remove_unused_layers no)
-			(net 679 "unconnected-(U9A-PA13-PadCN7_13)")
+			(net 678 "unconnected-(U9A-PA13-PadCN7_13)")
 			(pinfunction "PA13")
 			(pintype "bidirectional")
@@
 			(layers "*.Cu" "*.Mask")
 			(remove_unused_layers no)
-			(net 681 "unconnected-(U9A-PA14-PadCN7_15)")
+			(net 680 "unconnected-(U9A-PA14-PadCN7_15)")
 			(pinfunction "PA14")
 			(pintype "bidirectional")
@@
 			(layers "*.Cu" "*.Mask")
 			(remove_unused_layers no)
-			(net 675 "unconnected-(U9A-CN7_+3V3-PadCN7_16)")
+			(net 674 "unconnected-(U9A-CN7_+3V3-PadCN7_16)")
 			(pinfunction "CN7_+3V3")
-			(pintype "power_in")
+			(pintype "power_in+no_connect")
 			(solder_mask_margin 0.102)
 		)
@@
 			(layers "*.Cu" "*.Mask")
 			(remove_unused_layers no)
-			(net 673 "unconnected-(U9A-CN7_+5V-PadCN7_18)")
+			(net 672 "unconnected-(U9A-CN7_+5V-PadCN7_18)")
 			(pinfunction "CN7_+5V")
-			(pintype "power_in")
+			(pintype "power_in+no_connect")
 			(solder_mask_margin 0.102)
 		)
@@
 			(layers "*.Cu" "*.Mask")
 			(remove_unused_layers no)
-			(net 672 "Net-(U9A-CN7_GND-PadCN7_19)")
+			(net 690 "unconnected-(U9A-CN7_GND-PadCN7_19)_1")
 			(pinfunction "CN7_GND")
-			(pintype "power_in")
+			(pintype "power_in+no_connect")
 			(solder_mask_margin 0.102)
 		)
@@
 			(layers "*.Cu" "*.Mask")
 			(remove_unused_layers no)
-			(net 672 "Net-(U9A-CN7_GND-PadCN7_19)")
+			(net 689 "unconnected-(U9A-CN7_GND-PadCN7_19)")
 			(pinfunction "CN7_GND")
-			(pintype "power_in")
+			(pintype "power_in+no_connect")
 			(solder_mask_margin 0.102)
 		)
@@
 			(layers "*.Cu" "*.Mask")
 			(remove_unused_layers no)
-			(net 678 "unconnected-(U9A-PB7-PadCN7_21)")
+			(net 677 "unconnected-(U9A-PB7-PadCN7_21)")
 			(pinfunction "PB7")
 			(pintype "bidirectional")
@@
 			(layers "*.Cu" "*.Mask")
 			(remove_unused_layers no)
-			(net 672 "Net-(U9A-CN7_GND-PadCN7_19)")
+			(net 692 "unconnected-(U9A-CN7_GND-PadCN7_19)_3")
 			(pinfunction "CN7_GND")
-			(pintype "power_in")
+			(pintype "power_in+no_connect")
 			(solder_mask_margin 0.102)
 		)
@@
 			(layers "*.Cu" "*.Mask")
 			(remove_unused_layers no)
-			(net 680 "unconnected-(U9A-CN7_VIN-PadCN7_24)")
+			(net 679 "unconnected-(U9A-CN7_VIN-PadCN7_24)")
 			(pinfunction "CN7_VIN")
-			(pintype "power_in")
+			(pintype "power_in+no_connect")
 			(solder_mask_margin 0.102)
 		)
@@
 			(layers "*.Cu" "*.Mask")
 			(remove_unused_layers no)
-			(net 686 "unconnected-(U9A-PC15-PadCN7_27)")
+			(net 685 "unconnected-(U9A-PC15-PadCN7_27)")
 			(pinfunction "PC15")
 			(pintype "bidirectional")
@@
 			(layers "*.Cu" "*.Mask")
 			(remove_unused_layers no)
-			(net 682 "unconnected-(U9A-PA1-PadCN7_30)")
+			(net 681 "unconnected-(U9A-PA1-PadCN7_30)")
 			(pinfunction "PA1")
 			(pintype "bidirectional")
@@
 			(layers "*.Cu" "*.Mask")
 			(remove_unused_layers no)
-			(net 677 "unconnected-(U9A-VBAT-PadCN7_33)")
+			(net 676 "unconnected-(U9A-VBAT-PadCN7_33)")
 			(pinfunction "VBAT")
-			(pintype "power_in")
+			(pintype "power_in+no_connect")
 			(solder_mask_margin 0.102)
 		)
@@
 			(layers "*.Cu" "*.Mask")
 			(remove_unused_layers no)
-			(net 684 "unconnected-(U9A-PC2-PadCN7_35)")
+			(net 683 "unconnected-(U9A-PC2-PadCN7_35)")
 			(pinfunction "PC2")
 			(pintype "bidirectional")
@@
 			(layers "*.Cu" "*.Mask")
 			(remove_unused_layers no)
-			(net 685 "unconnected-(U9B-PC7-PadCN10_19)")
+			(net 684 "unconnected-(U9B-PC7-PadCN10_19)")
 			(pinfunction "PC7")
 			(pintype "bidirectional")
@@
 			(net 554 "unconnected-(U31-Vref-Pad5)")
 			(pinfunction "Vref")
-			(pintype "power_out+no_connect")
+			(pintype "power_out")
 		)
 		(pad "6" thru_hole circle
@@
 			(net 553 "unconnected-(U30-Vref-Pad5)")
 			(pinfunction "Vref")
-			(pintype "power_out+no_connect")
+			(pintype "power_out")
 		)
 		(pad "6" thru_hole circle
